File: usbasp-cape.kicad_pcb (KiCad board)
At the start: 2 copper layers, 86.4 x 54.6 mm, 24 parts, among them P1 CONN_2, P2 CONN_2, P3 CONN_2, P4 CONN_2, P5 CONN_5X2, P6 CONN_5X2, U1 BEAGLEBONEBLACK, U2 SN74CBTLV3253, U3 SN74CBTLV3253, U4 INA219

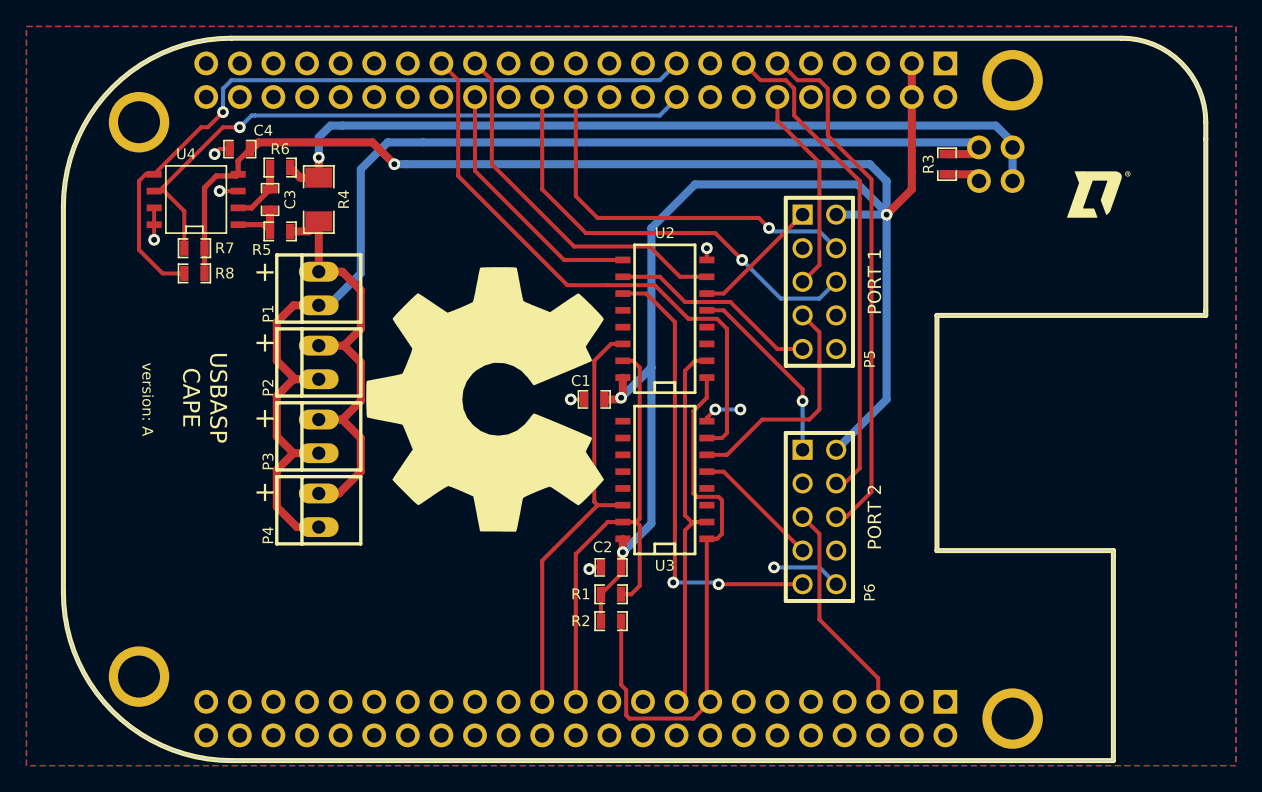
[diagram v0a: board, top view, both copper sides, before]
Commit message: reworked ground fills
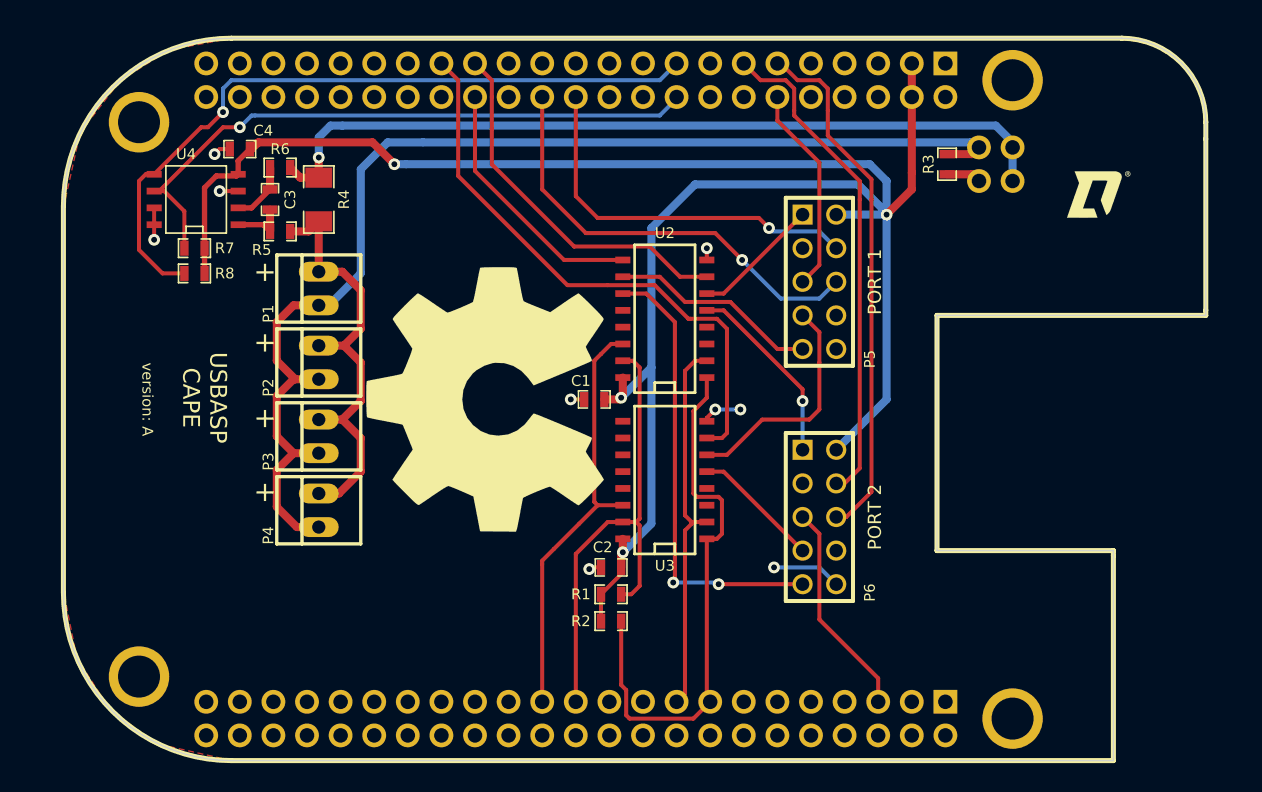
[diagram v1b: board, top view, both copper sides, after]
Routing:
- removed copper zone on B.Cu, net GND
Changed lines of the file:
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@@
   (general
     (links 83)
-    (no_connects 0)
-    (area 103.886 70.866 195.326001 126.758701)
+    (no_connects 1)
+    (area 106.286299 71.361299 193.433701 126.758701)
     (thickness 1.6)
     (drawings 8)
@@
   (title_block
     (title "BeagleBone Black USBASP Cape")
-    (date "01 sept  2014")
+    (date "02 sept  2014")
     (rev A)
     (company Defendec)
@@
       (linewidth 0.020000)
       (plotframeref false)
-      (viasonmask false)
+      (viasonmask true)
       (mode 1)
       (useauxorigin false)
@@
       (drillshape 0)
       (scaleselection 1)
-      (outputdirectory gerbers/))
+      (outputdirectory ""))
   )
   (net 0 "")
@@
     (polygon
       (pts
-        (xy 195.326 126.746) (xy 103.886 126.746) (xy 103.886 70.866) (xy 195.326 70.866)
+        (xy 193.04 92.71) (xy 172.72 92.71) (xy 172.72 110.49) (xy 186.055 110.49) (xy 186.055 126.365)
+        (xy 119.38 126.365) (xy 113.792 125.095) (xy 110.236 122.555) (xy 107.696 118.618) (xy 106.68 113.538)
+        (xy 106.68 84.582) (xy 107.95 78.867) (xy 110.998 74.93) (xy 114.681 72.644) (xy 119.38 71.755)
+        (xy 186.563 71.755) (xy 189.103 72.263) (xy 191.389 73.787) (xy 192.659 75.946) (xy 193.04 78.105)
       )
     )
-  )
-  (zone (net 7) (net_name GND) (layer B.Cu) (hatch edge 0.508)
-    (connect_pads (clearance 0.2032))
-    (min_thickness 0.254)
-    (fill (arc_segments 16) (thermal_gap 0.508) (thermal_bridge_width 0.508))
-    (polygon
-      (pts
-        (xy 195.326 126.746) (xy 103.886 126.746) (xy 103.886 70.866) (xy 195.326 70.866)
-      )
-    )
